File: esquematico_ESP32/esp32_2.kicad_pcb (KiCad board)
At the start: 2 copper layers, 79.6 x 93.5 mm, 42 parts, among them J2 Conn_RFID1, J3 Conn_RFID2, J4 USB_A, J5 Conn_screen, J6 Conn_01x04_Female, J7 Jack-DC, Q1 BSS138, Q2 BSS138, SW1 SW_Push, SW2 Enable, U1 ESP32-WROOM-32, U2 LM1117-3.3, U3 LM2596S-5

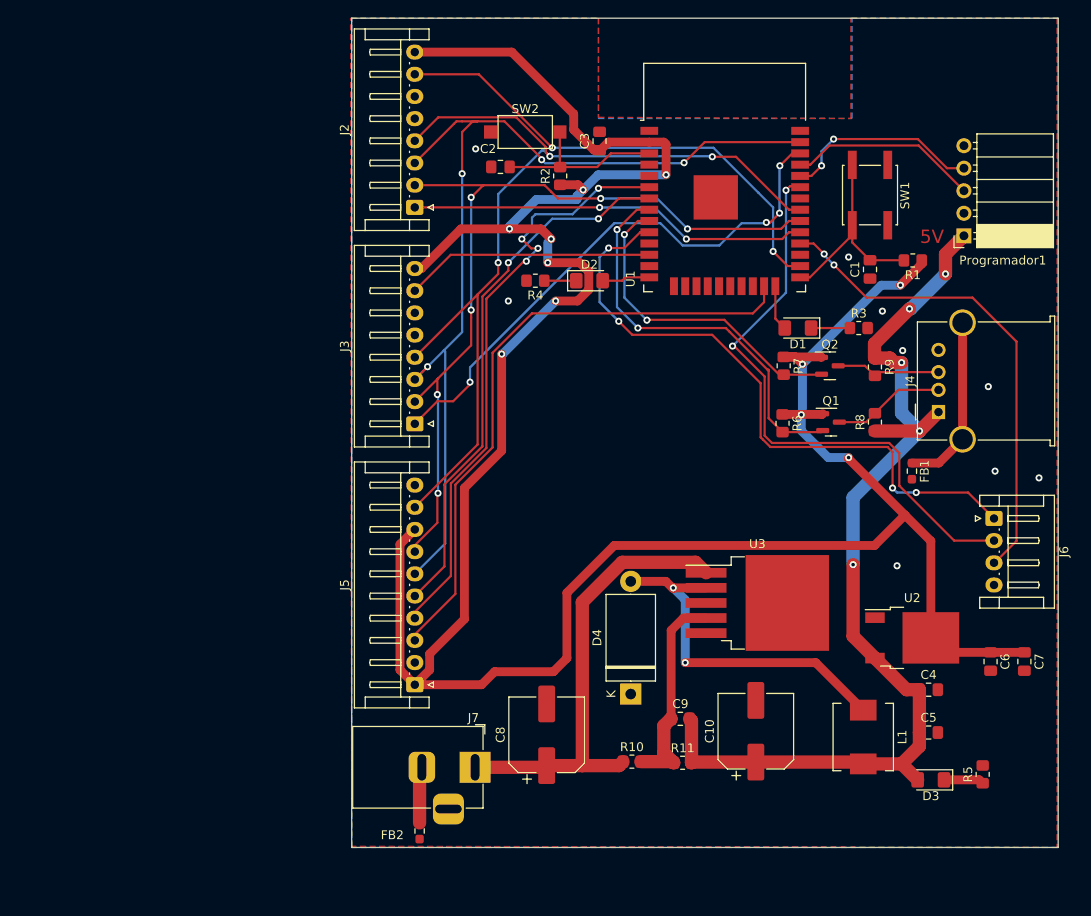
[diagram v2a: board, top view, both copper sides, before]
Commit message: correción de un pulsador
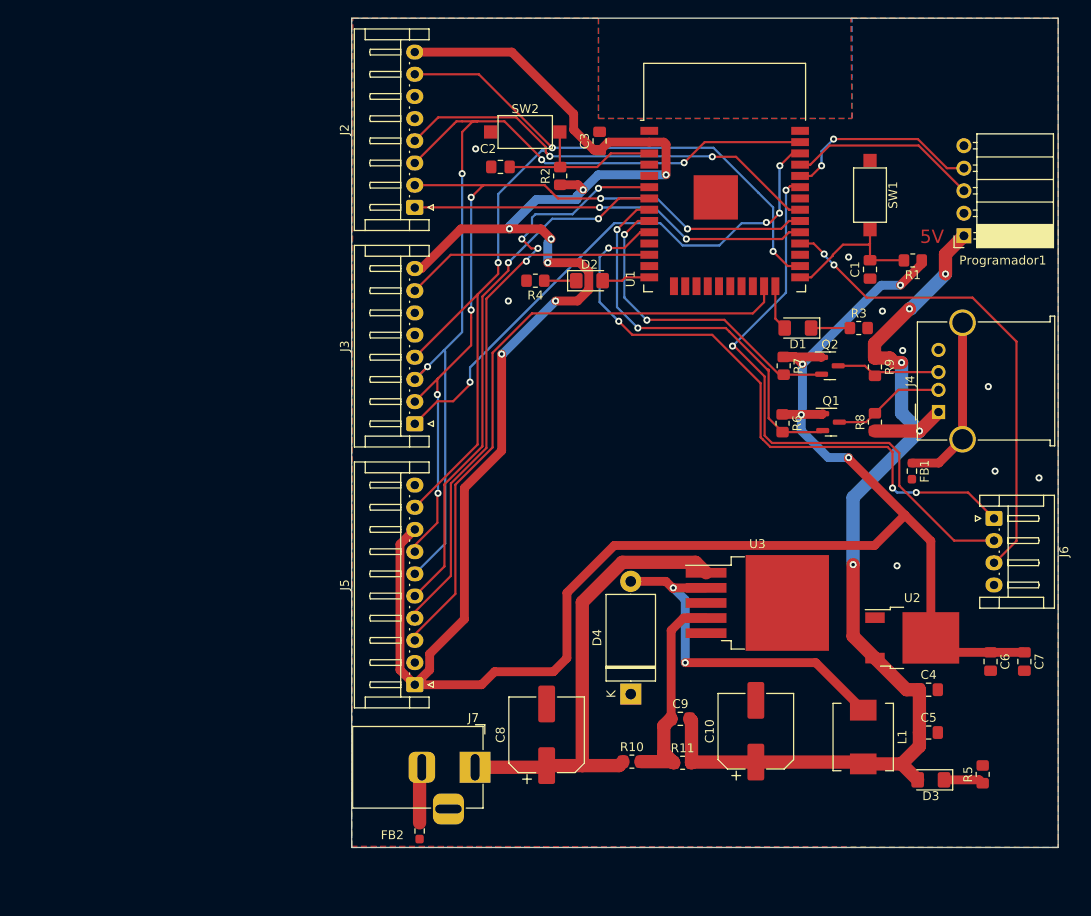
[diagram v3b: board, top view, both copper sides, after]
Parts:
- SW1: footprint Button_Switch_SMD:SW_SPST_EVQQ2 -> Button_Switch_SMD:SW_SPST_CK_RS282G05A3
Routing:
- net /IOD: track 24.4 -> 16.8 mm
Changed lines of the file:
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@@
     )
   )
-  (footprint "Button_Switch_SMD:SW_SPST_EVQQ2" (layer "F.Cu")
+  (footprint "Button_Switch_SMD:SW_SPST_CK_RS282G05A3" (layer "F.Cu")
     (at 188.722 48.006 -90)
-    (descr "Light Touch Switch, https://industrial.panasonic.com/cdbs/www-data/pdf/ATK0000/ATK0000CE28.pdf")
+    (descr "https://www.mouser.com/ds/2/60/RS-282G05A-SM_RT-1159762.pdf")
+    (tags "SPST button tactile switch")
     (property "Sheetfile" "esp32_2.kicad_sch")
     (property "Sheetname" "")
     (attr smd)
-    (fp_text reference "SW1" (at 0.05 -3.95 -90) (layer "F.SilkS")
-      (effects (font (size 1 1) (thickness 0.15)))
-    )
-    (fp_text value "SW_Push" (at 0 4.25 -90) (layer "F.Fab")
-      (effects (font (size 1 1) (thickness 0.15)))
-    )
-    (fp_text user "${REFERENCE}" (at 0.05 -3.95 -90) (layer "F.Fab")
-      (effects (font (size 1 1) (thickness 0.15)))
-    )
-    (fp_line (start -3.35 3.1) (end 3.35 3.1) (layer "F.SilkS") (width 0.12))
-    (fp_line (start 3.35 -1.2) (end 3.35 1.2) (layer "F.SilkS") (width 0.12))
-    (fp_line (start -3.35 -1.2) (end -3.35 1.2) (layer "F.SilkS") (width 0.12))
-    (fp_line (start 3.35 -3.1) (end 3.35 -2.9) (layer "F.SilkS") (width 0.12))
-    (fp_line (start -3.35 -3.1) (end -3.35 -2.9) (layer "F.SilkS") (width 0.12))
-    (fp_line (start -3.35 3.1) (end -3.35 2.9) (layer "F.SilkS") (width 0.12))
-    (fp_line (start 3.35 3.1) (end 3.35 2.9) (layer "F.SilkS") (width 0.12))
-    (fp_line (start 3.35 -3.1) (end -3.35 -3.1) (layer "F.SilkS") (width 0.12))
-    (fp_line (start -5.25 -3.25) (end 5.25 -3.25) (layer "F.CrtYd") (width 0.05))
-    (fp_line (start 5.25 -3.25) (end 5.25 3.25) (layer "F.CrtYd") (width 0.05))
-    (fp_line (start -5.25 3.25) (end -5.25 -3.25) (layer "F.CrtYd") (width 0.05))
-    (fp_line (start 5.25 3.25) (end -5.25 3.25) (layer "F.CrtYd") (width 0.05))
-    (fp_line (start -3.25 -3) (end 3.25 -3) (layer "F.Fab") (width 0.1))
-    (fp_line (start -3.25 3) (end -3.25 -3) (layer "F.Fab") (width 0.1))
-    (fp_line (start 3.25 -3) (end 3.25 3) (layer "F.Fab") (width 0.1))
-    (fp_line (start 3.25 3) (end -3.25 3) (layer "F.Fab") (width 0.1))
-    (fp_circle (center 0 0) (end 1.9 0) (layer "F.Fab") (width 0.1) (fill none))
-    (fp_circle (center 0 0) (end 1.5 0) (layer "F.Fab") (width 0.1) (fill none))
-    (pad "1" smd rect (at 3.4 -2 270) (size 3.2 1) (layers "F.Cu" "F.Paste" "F.Mask")
+    (fp_text reference "SW1" (at 0 -2.6 -90) (layer "F.SilkS")
+      (effects (font (size 1 1) (thickness 0.15)))
+    )
+    (fp_text value "SW_Push" (at 0 3 -90) (layer "F.Fab")
+      (effects (font (size 1 1) (thickness 0.15)))
+    )
+    (fp_text user "${REFERENCE}" (at 0 -2.6 -90) (layer "F.Fab")
+      (effects (font (size 1 1) (thickness 0.15)))
+    )
+    (fp_line (start 3.06 1.85) (end -3.06 1.85) (layer "F.SilkS") (width 0.12))
+    (fp_line (start -3.06 1.85) (end -3.06 -1.85) (layer "F.SilkS") (width 0.12))
+    (fp_line (start -3.06 -1.85) (end 3.06 -1.85) (layer "F.SilkS") (width 0.12))
+    (fp_line (start 3.06 -1.85) (end 3.06 1.85) (layer "F.SilkS") (width 0.12))
+    (fp_line (start -4.9 2.05) (end -4.9 -2.05) (layer "F.CrtYd") (width 0.05))
+    (fp_line (start 4.9 2.05) (end -4.9 2.05) (layer "F.CrtYd") (width 0.05))
+    (fp_line (start 4.9 -2.05) (end 4.9 2.05) (layer "F.CrtYd") (width 0.05))
+    (fp_line (start -4.9 -2.05) (end 4.9 -2.05) (layer "F.CrtYd") (width 0.05))
+    (fp_line (start -3 1.8) (end 3 1.8) (layer "F.Fab") (width 0.1))
+    (fp_line (start -1.5 0.8) (end 1.5 0.8) (layer "F.Fab") (width 0.1))
+    (fp_line (start 1.75 -1) (end 1.75 1) (layer "F.Fab") (width 0.1))
+    (fp_line (start -1.75 1) (end -1.75 -1) (layer "F.Fab") (width 0.1))
+    (fp_line (start -1.75 -1) (end 1.75 -1) (layer "F.Fab") (width 0.1))
+    (fp_line (start 3 -1.8) (end 3 1.8) (layer "F.Fab") (width 0.1))
+    (fp_line (start 1.75 1) (end -1.75 1) (layer "F.Fab") (width 0.1))
+    (fp_line (start -1.5 -0.8) (end 1.5 -0.8) (layer "F.Fab") (width 0.1))
+    (fp_line (start 1.5 -0.8) (end 1.5 0.8) (layer "F.Fab") (width 0.1))
+    (fp_line (start -1.5 -0.8) (end -1.5 0.8) (layer "F.Fab") (width 0.1))
+    (fp_line (start -3 -1.8) (end 3 -1.8) (layer "F.Fab") (width 0.1))
+    (fp_line (start -3 -1.8) (end -3 1.8) (layer "F.Fab") (width 0.1))
+    (pad "1" smd rect (at -3.9 0 270) (size 1.5 1.5) (layers "F.Cu" "F.Paste" "F.Mask")
       (net 4 "GND") (pinfunction "1") (pintype "passive"))
-    (pad "1" smd rect (at -3.4 -2 270) (size 3.2 1) (layers "F.Cu" "F.Paste" "F.Mask")
-      (net 4 "GND") (pinfunction "1") (pintype "passive"))
-    (pad "2" smd rect (at -3.4 2 270) (size 3.2 1) (layers "F.Cu" "F.Paste" "F.Mask")
+    (pad "2" smd rect (at 3.9 0 270) (size 1.5 1.5) (layers "F.Cu" "F.Paste" "F.Mask")
       (net 7 "/IOD") (pinfunction "2") (pintype "passive"))
-    (pad "2" smd rect (at 3.4 2 270) (size 3.2 1) (layers "F.Cu" "F.Paste" "F.Mask")
-      (net 7 "/IOD") (pinfunction "2") (pintype "passive"))
-    (model "${KICAD6_3DMODEL_DIR}/Button_Switch_SMD.3dshapes/SW_SPST_EVQQ2.wrl"
+    (model "${KICAD6_3DMODEL_DIR}/Button_Switch_SMD.3dshapes/SW_SPST_CK_RS282G05A3.wrl"
       (offset (xyz 0 0 0))
       (scale (xyz 1 1 1))
@@
   (segment (start 192.278 66.88648) (end 192.278 72.572) (width 1.5) (layer "B.Cu") (net 6))
   (segment (start 193.294 60.833) (end 197.231 56.896) (width 1.5) (layer "B.Cu") (net 6))
-  (segment (start 186.722 51.406) (end 186.722 52.506) (width 0.25) (layer "F.Cu") (net 7))
+  (segment (start 184.531 54.835) (end 184.531 54.737) (width 0.25) (layer "F.Cu") (net 7))
+  (segment (start 188.722 53.467) (end 188.722 51.906) (width 0.25) (layer "F.Cu") (net 7))
   (segment (start 192.5265 55.3505) (end 192.548 55.372) (width 0.25) (layer "F.Cu") (net 7))
-  (segment (start 181.951 57.277) (end 180.839 57.277) (width 0.25) (layer "F.Cu") (net 7))
-  (segment (start 186.722 53.3505) (end 186.722 51.406) (width 0.25) (layer "F.Cu") (net 7))
-  (segment (start 186.722 44.606) (end 186.722 51.406) (width 0.25) (layer "F.Cu") (net 7))
-  (segment (start 186.722 52.506) (end 181.951 57.277) (width 0.25) (layer "F.Cu") (net 7))
+  (segment (start 185.674 53.594) (end 188.595 53.594) (width 0.25) (layer "F.Cu") (net 7))
+  (segment (start 182.089 57.277) (end 184.531 54.835) (width 0.25) (layer "F.Cu") (net 7))
+  (segment (start 180.839 57.277) (end 182.089 57.277) (width 0.25) (layer "F.Cu") (net 7))
+  (segment (start 188.595 53.594) (end 188.722 53.467) (width 0.25) (layer "F.Cu") (net 7))
   (segment (start 188.722 55.3505) (end 192.5265 55.3505) (width 0.25) (layer "F.Cu") (net 7))
-  (segment (start 188.722 55.3505) (end 186.722 53.3505) (width 0.25) (layer "F.Cu") (net 7))
+  (segment (start 188.722 55.3505) (end 188.722 53.467) (width 0.25) (layer "F.Cu") (net 7))
+  (segment (start 184.531 54.737) (end 185.674 53.594) (width 0.25) (layer "F.Cu") (net 7))
   (segment (start 160.791511 89.398489) (end 156.291 93.899) (width 1.5) (layer "F.Cu") (net 8))
   (segment (start 152.084 112.503) (end 152.273 112.314) (width 1.5) (layer "F.Cu") (net 8))
@@
     (polygon
       (pts
-        (xy 158.115 39.243)
-        (xy 186.563 39.37)
+        (xy 158.115 39.37)
+        (xy 186.69 39.37)
         (xy 186.563 28.067)
-        (xy 209.804 28.067)
-        (xy 209.804 121.539)
+        (xy 209.931 28.067)
+        (xy 209.931 121.539)
         (xy 130.302 121.412)
-        (xy 130.175 28.067)
+        (xy 130.429 28.067)
         (xy 158.115 28.067)
       )

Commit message: .
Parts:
- removed C9: C, Capacitor_SMD:C_0805_2012Metric_Pad1.18x1.45mm_HandSolder
- removed R10, R11: R, Resistor_SMD:R_0805_2012Metric_Pad1.20x1.40mm_HandSolder
- C1, C2: value C -> 1nf
- C10: value C_Polarized -> 220u
- C3: value C_Polarized -> 100u
- C4, C7: value C -> 100n
- C5: value C -> 10u
- C6: value C -> 22u
- C8: value C_Polarized -> 470u
- D4: value DIODE -> 1N5825
- L1: value L -> 68u
- R1, R2, R3, R4, R5, R6, R7, R8, R9: value R -> 10k
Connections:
- U3 pad 4: Net-(C9-Pad1) -> +5V
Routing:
- net Net-(C9-Pad1): track 24.0 -> 0.00 mm
- net +5V: track 114.7 -> 129.0 mm
- net +12V: track 51.7 -> 46.9 mm

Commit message: .
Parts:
- moved D4 3.70 mm to (161.8, 108.0)
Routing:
- net /RST_1: track 55.3 -> 58.3 mm
- net /SCK: track 94.3 -> 96.5 mm
- net /MISO: track 106.6 -> 107.8 mm
- net /CS_LECTOR_1: track 45.2 -> 46.2 mm
- net +12V: track 46.9 -> 45.9 mm
- net Net-(D4-Pad2): track 40.1 -> 41.0 mm
- net /CS_LECTOR_2: track 62.3 -> 63.2 mm

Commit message: .
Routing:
- net /CS_LECTOR_2: track 63.2 -> 66.0 mm
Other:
- board text added: "3V3"
- board text added: "CS"
- board text added: "CS1"
- board text added: "CS2"
- board text added: "D/C"
- board text added: "GND"
- board text added: "M1"
- board text added: "M2"
- board text added: "M3"
- board text added: "MISO"
- board text added: "MOSI"
- board text added: "RST"
- board text added: "RX"
- board text added: "SCK"
- board text added: "TX"

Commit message: diseño listo
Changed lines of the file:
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@@
   (segment (start 167.894 100.711) (end 167.894 93.628) (width 1) (layer "B.Cu") (net 46))
   (segment (start 167.894 93.628) (end 166.546 92.28) (width 1) (layer "B.Cu") (net 46))
-  (zone (net 0) (net_name "") (layers F&B.Cu) (hatch edge 0.508)
-    (connect_pads (clearance 0))
-    (min_thickness 0.254)
-    (keepout (tracks not_allowed) (vias not_allowed) (pads not_allowed ) (copperpour not_allowed) (footprints not_allowed))
-    (fill (thermal_gap 0.508) (thermal_bridge_width 0.508))
-    (polygon
-      (pts
-        (xy 186.563 39.243)
-        (xy 158.115 39.243)
-        (xy 158.115 28.067)
-        (xy 186.563 28.067)
-      )
-    )
-  )
   (zone (net 4) (net_name "GND") (layer "F.Cu") (hatch edge 0.508)
     (connect_pads (clearance 0.508))
@@
     (polygon
       (pts
-        (xy 158.115 39.37)
-        (xy 186.69 39.37)
-        (xy 186.563 28.067)
+        (xy 157.9118 39.37)
+        (xy 186.888609 39.367768)
+        (xy 186.761609 28.064768)
         (xy 209.931 28.067)
         (xy 209.931 121.539)
         (xy 130.302 121.412)
         (xy 130.429 28.067)
-        (xy 158.115 28.067)
+        (xy 157.9118 28.067)
       )
     )
@@
     (polygon
       (pts
-        (xy 158.115 39.37)
+        (xy 158.0134 39.37)
         (xy 186.69 39.37)
         (xy 186.69 28.067)
@@
         (xy 130.302 121.539)
         (xy 130.302 28.067)
-        (xy 158.115 28.067)
+        (xy 158.0134 28.067)
       )
     )

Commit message: Correciones de la clase
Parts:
- removed Programador1: Conn_01x05_Female, Connector_PinSocket_2.54mm:PinSocket_1x05_P2.54mm_Horizontal
- added Programador: Conn_01x05_Female, Connector_PinSocket_2.54mm:PinSocket_1x05_P2.54mm_Horizontal, F.Cu at (199.6, 52.9)
- added Verificación: Conn_01x03_Male, Connector_PinHeader_2.54mm:PinHeader_1x03_P2.54mm_Vertical, F.Cu at (183.9, 82.3)
- moved C2 52.7 mm to (198.4, 56.5), turned to 90 degrees
- moved SW2 44.2 mm to (193.4, 48.0), turned to -90 degrees
- moved R2 41.1 mm to (193.5, 56.4)
- moved FB2 9.74 mm to (147.6, 118.6), turned to 180 degrees
- moved R1 8.59 mm to (185.0, 56.3), turned to 90 degrees
- moved SW1 1.12 mm to (187.6, 48.0)
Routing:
- net +3V3: track 308.2 -> 356.8 mm, vias 11 -> 13
- net /EN: track 20.3 -> 51.7 mm, vias 0 -> 4
- net +5V: track 129.0 -> 114.0 mm, vias 5 -> 3
- net Net-(FB2-Pad2): track 6.37 -> 12.4 mm
- net /IOD: track 16.8 -> 11.9 mm
- net /MAGNE_1: track 55.1 -> 57.3 mm
- net GND: vias 9 -> 31
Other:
- board text added: "3.3V"
